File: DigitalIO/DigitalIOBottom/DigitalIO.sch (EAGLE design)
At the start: 75 parts, among them IC1 MCP23017SP, IC2 ULN2803A, K5 HF46105, K6 HF46105, K7 HF46105, K8 HF46105, P1 DF11-06-2DS, Q1 BS170, Q2 BS170, Q3 BS170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

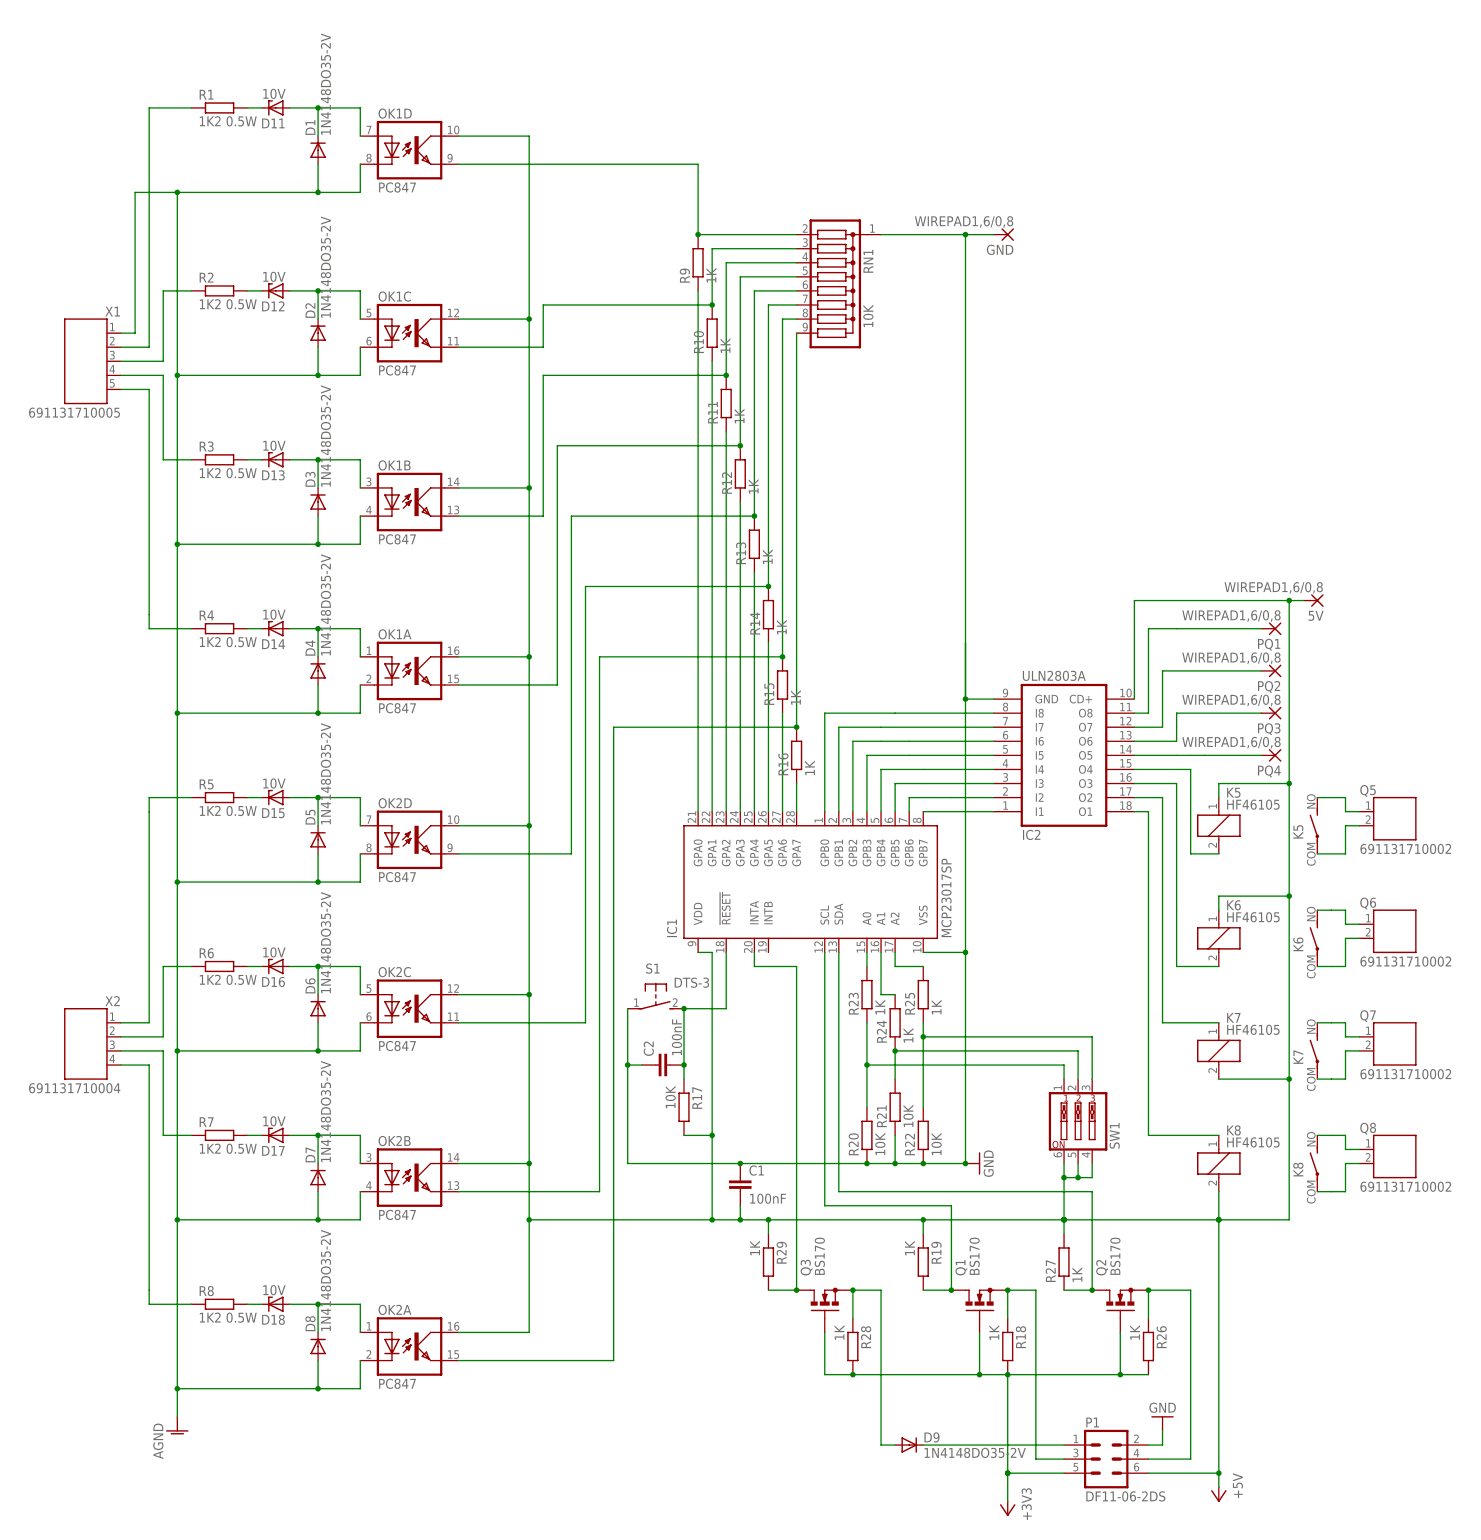
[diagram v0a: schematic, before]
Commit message: Rework to operate with 5V only. Add INT and RESET signals.
Signed-off-by: Alexander Falkenstern <alexander.falkenstern@gmail.com>
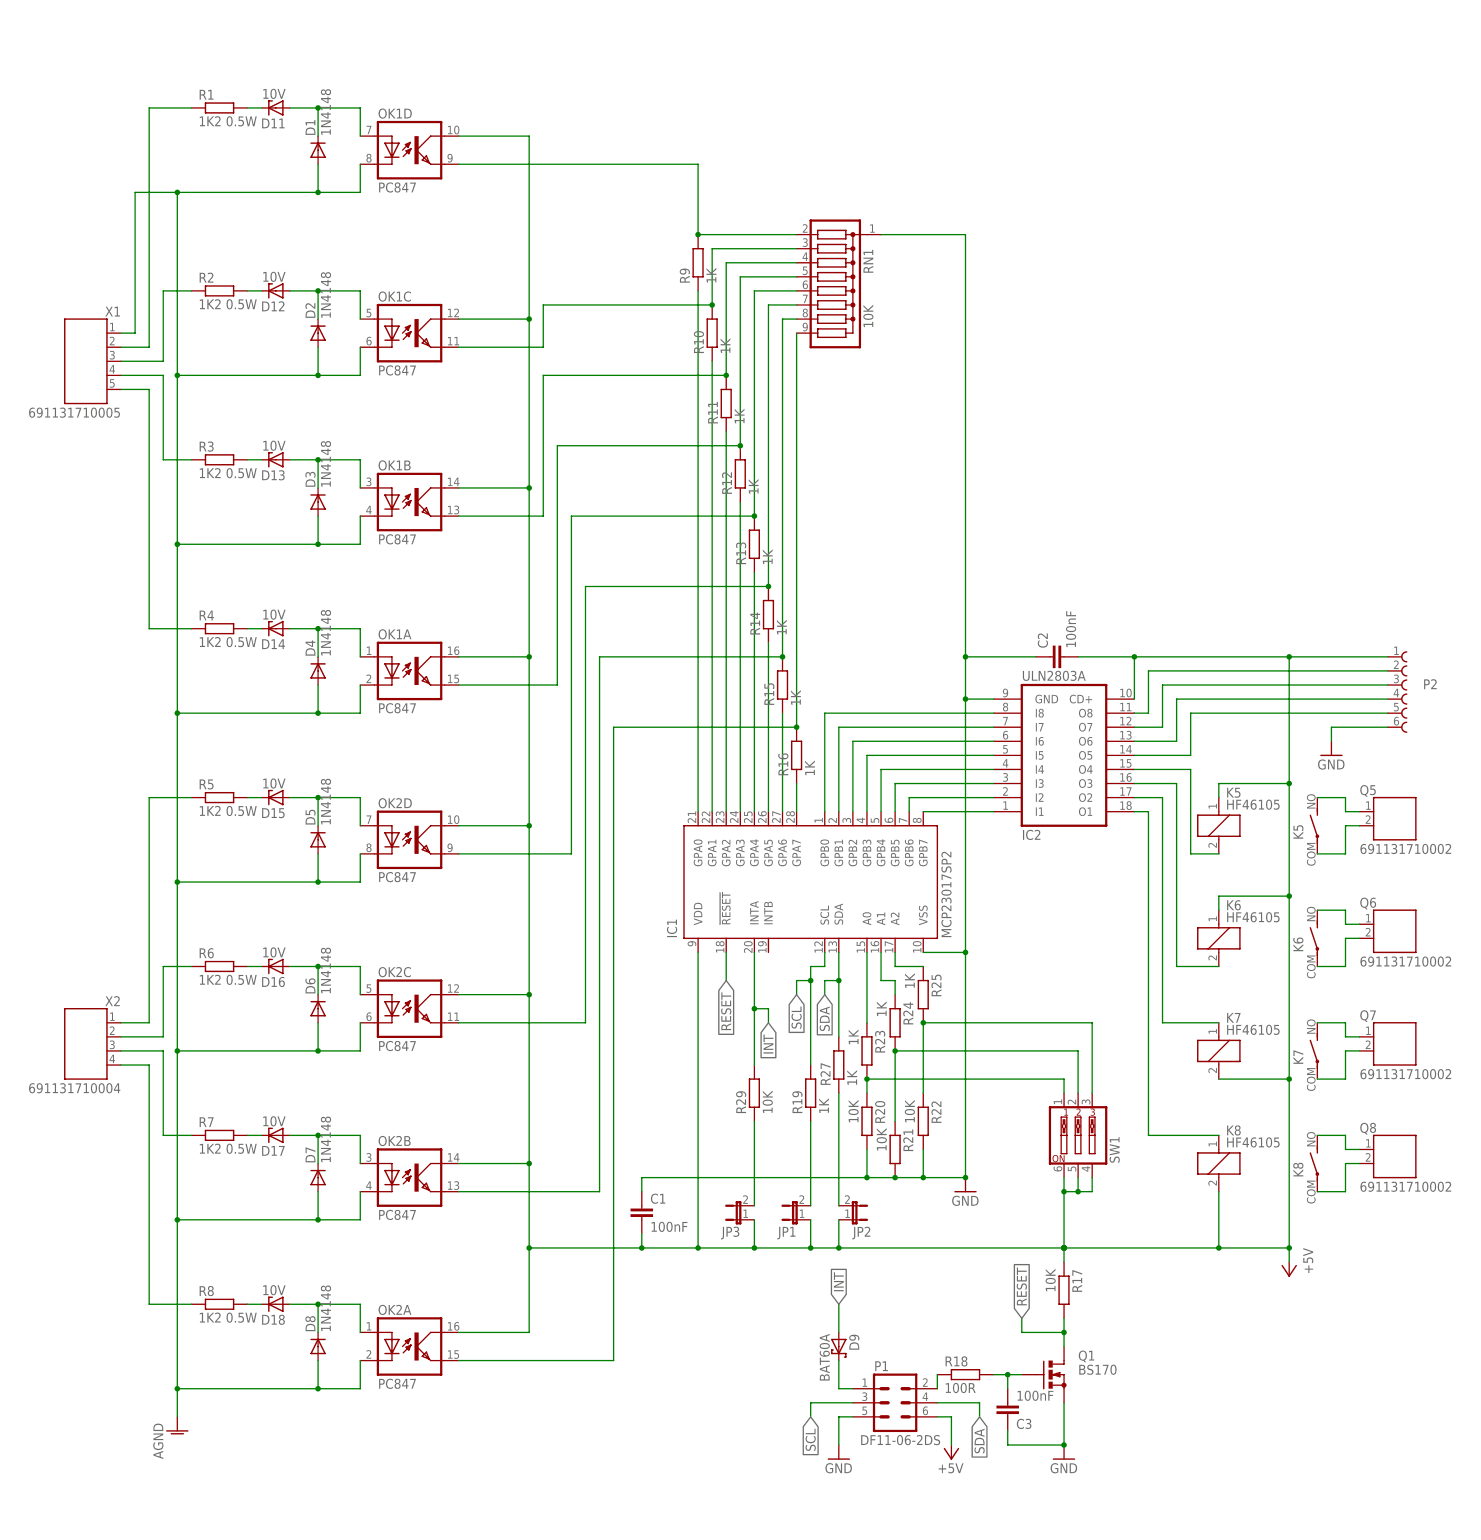
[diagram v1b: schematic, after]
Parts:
- removed 5V, GND, PQ1, PQ2, PQ3, PQ4: WIREPAD1,6/0,8, wirepad:WIREPAD1,6/0,8
- removed Q2, Q3: BS170, transistor-small-signal:BS170
- removed R26, R28: 1K, rcl:R-EU_0204/2V
- removed S1: DTS-3, switch-tact:DTS-3
- added C3: 100nF, rcl:C-EUC0805
- added JP1, JP2, JP3: (no value), jumper:JP1E
- added P2: 62000611121, Board_to_Board_Connectors_rev15d:62000611121
- D1, D2, D3, D4, D5, D6, D7, D8: value 1N4148DO35-2V -> 1N4148
- D9: value 1N4148DO35-2V -> BAT60A; device diode:1N4148DO35-2V -> diode:BAT60J; OC_FARNELL unknown -> (none)
- IC1: value MCP23017SP -> MCP23017SP2; device mcp:MCP23017SP -> mcp:MCP23017SP2
- IC2: device uln-udn:ULN2803A -> uln-udn:ULN2803ASP2
- Q1: MF ON SEMICONDUCTOR -> (none); MPN BS170G -> (none); OC_FARNELL 9556192 -> (none)
- R18: value 1K -> 100R; device rcl:R-EU_0204/2V -> resistor:R-EU_0204/2V
- R29: value 1K -> 10K
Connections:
- removed net +3V3: P1.5, Q1.G, Q2.G, Q3.G, R18.2, R26.2, R28.2
- removed net N$57: C2.2, IC1.!RESET, R17.1, S1.2
- removed net N$81: IC1.INTA, Q3.D, R29.2
- new net INT: D9.A, IC1.INTA, R29.2
- new net RESET: IC1.!RESET, Q1.D, R17.2
- new net SCL: IC1.SCL, P1.3, R19.2
- new net SDA: IC1.SDA, P1.4, R27.2
- net +5V: now also C2.2, JP1.1, JP2.1, JP3.1, P2.1, R17.1; no longer 5V.P, R17.2, R19.1, R27.2, R29.1
- net GND: now also C3.1, P1.5, P2.6, Q1.S, R20.2, R21.2, R22.2; no longer GND.P, P1.2, R20.1, R21.1, R22.1, S1.1
- net N$11: now also R22.1, R25.2; no longer R22.2, R25.1
- net N$28: now also P2.5; no longer PQ4.P
- net N$30: now also P2.4; no longer PQ3.P
- net N$32: now also P2.3; no longer PQ2.P
- net N$34: now also P2.2; no longer PQ1.P
- net N$36: now also JP2.2, R27.1; no longer D9.A, Q3.S, R28.1
- net N$50: now also R23.1; no longer R23.2
- net N$52: now also R24.1; no longer R24.2
- net N$58: now also JP3.2, R29.1; no longer IC1.SCL, Q1.D, R19.2
- net N$61: now also JP1.2, R19.1; no longer IC1.SDA, Q2.D, R27.1
- net N$69: now also P1.2, R18.1; no longer P1.4, Q2.S, R26.1
- net N$71: now also C3.2, Q1.G, R18.2; no longer P1.3, Q1.S, R18.1
- net N$77: now also R20.1, R23.2; no longer R20.2, R23.1
- net N$78: now also R21.1, R24.2; no longer R21.2, R24.1
- net N$79: now also R25.1; no longer R25.2
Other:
- moved on the sheet: C1, C2, P1, Q1, R17, R18, R19, R20, R21, R22, R23, R24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
